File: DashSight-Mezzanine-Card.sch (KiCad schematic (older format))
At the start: 60 parts, among them IC1 ELM327, J1 OBD2-DB9_Male, P1 CONN_02X20, Q1 2N3904, Q2 2N3906, Q3 2N3906, Q4 2N3904, Q5 2N3904, Q6 2N3904, Q7 2N3904, U1 MCP2561-E/P, U2 LM317L_TO92, Y1 4.0MHz

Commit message: sch: Update for the new Pine board
Signed-off-by: Alistair Francis <alistair@alistair23.me>
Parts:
- removed LD1, LD2, LD3, LD4, LD5: LD_1C2A, Opto-Devices:LaserDiode_TO3.3(D3.3)-3, symbol Device:Laserdiode_1C2A
- removed P1: CONN_02X20, 96boards:Pin_Header_Straight_2x20_Pitch2mm, symbol DashSight-Mezzanine-Card-rescue:CONN_02X20
- removed R1, R22, R23, R24, R29: 470, Resistors_SMD:R_0603_HandSoldering, symbol Device:R
- added J?: Pi2 Connector, symbol Connector_Generic:Conn_02x20_Odd_Even
- added J?: Euler Connector, symbol Connector_Generic:Conn_02x17_Odd_Even
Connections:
- net labels added: +3.3V, UART2_RX, UART2_TX, UART3_RX, UART3_TX
- net labels removed: UART0_RX, UART0_TX
- wire segments 174 -> 151
- no-connect marks 34 -> 1
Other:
- note removed: "96-Boards Pin Header"
- moved on the sheet: C1, C2, C3, C4, C5, C6, D1, D2, D3, D4, IC1, J1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

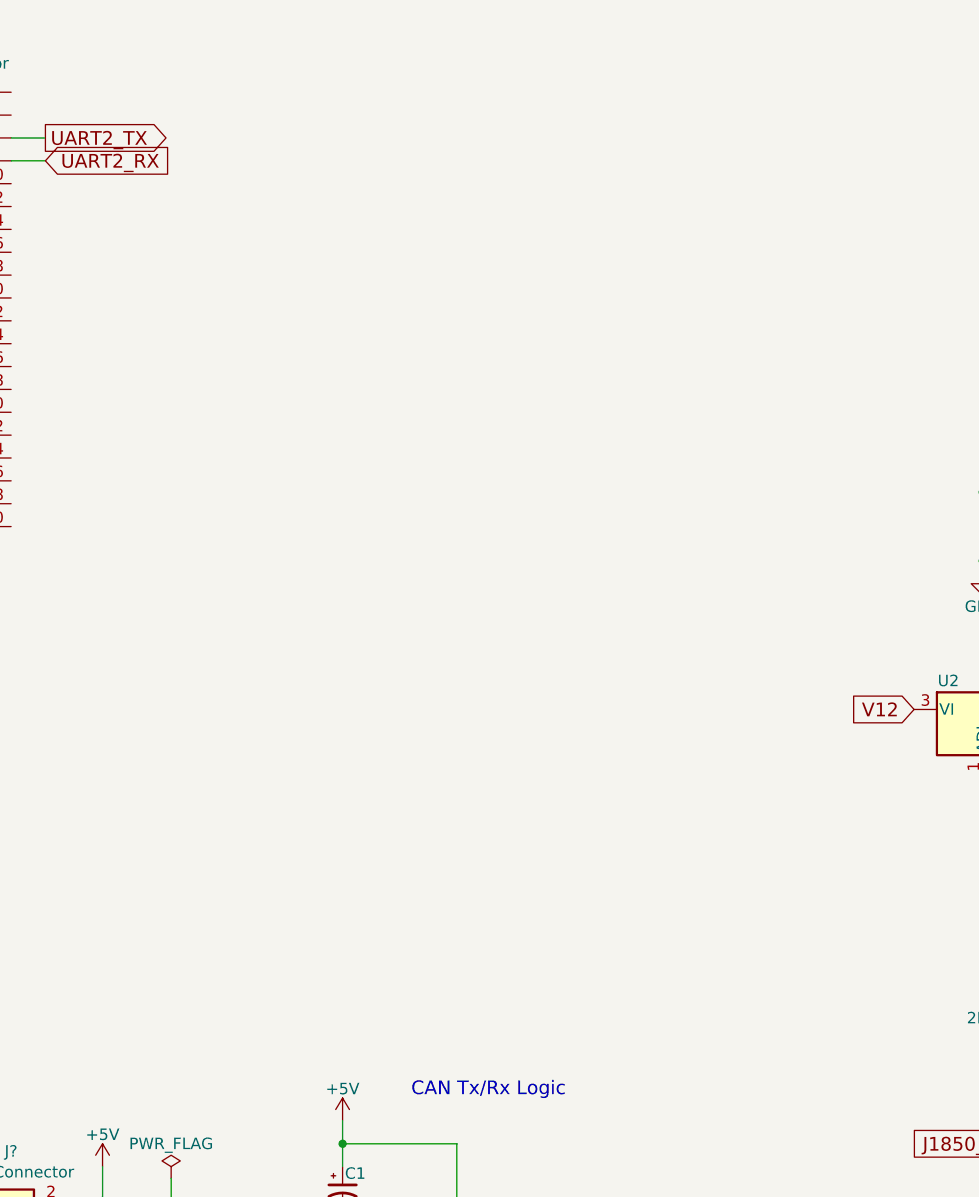
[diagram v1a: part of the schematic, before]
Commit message: Update with the GPS IC
Signed-off-by: Alistair Francis <alistair@alistair23.me>
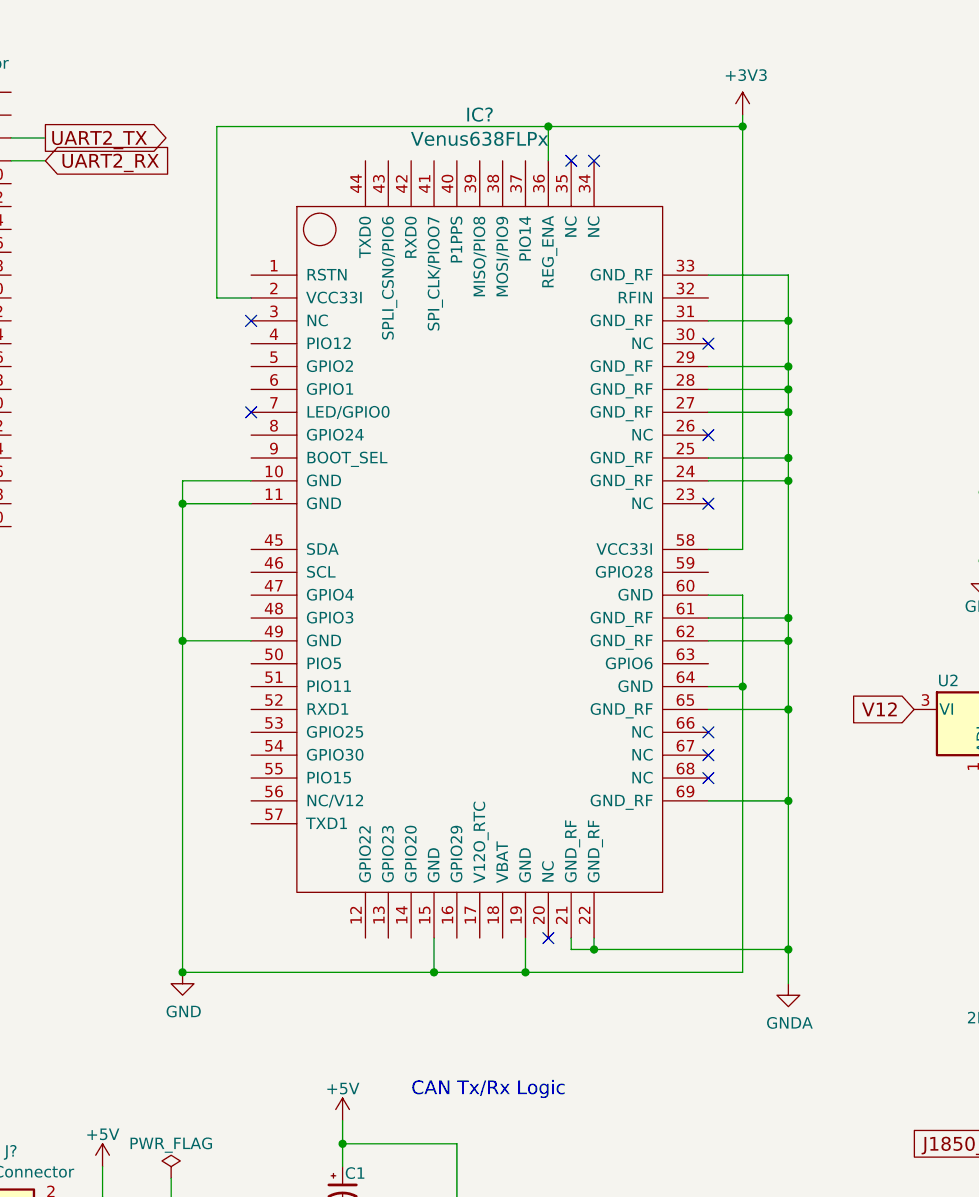
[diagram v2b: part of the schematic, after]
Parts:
- added IC?: Venus638FLPx, symbol Venus638FLPx:Venus638FLPx
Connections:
- net +3V3: now also IC?.2 (VCC33I), IC?.36 (REG_ENA), IC?.58 (VCC33I)
- net GND: now also IC?.10 (GND), IC?.11 (GND), IC?.15 (GND), IC?.19 (GND), IC?.49 (GND), IC?.60 (GND), IC?.64 (GND)
- new net GNDA: IC?.21 (GND_RF), IC?.22 (GND_RF), IC?.24 (GND_RF), IC?.25 (GND_RF), IC?.27 (GND_RF), IC?.28 (GND_RF), IC?.29 (GND_RF), IC?.31 (GND_RF), IC?.33 (GND_RF), IC?.61 (GND_RF), IC?.62 (GND_RF), IC?.65 (GND_RF), IC?.69 (GND_RF)
- no-connect marks 1 -> 12
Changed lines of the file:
@@
 	2650 7100 2650 7200
 Connection ~ 6750 6350
+$Comp
+L Venus638FLPx:Venus638FLPx IC?
+U 1 1 5BF87A18
+P 3450 3000
+F 0 "IC?" H 3450 5000 60  0000 C CNN
+F 1 "Venus638FLPx" H 3450 4894 60  0000 C CNN
+F 2 "" H 3450 3100 60  0001 C CNN
+F 3 "" H 3450 3100 60  0001 C CNN
+	1    3450 3000
+	1    0    0    -1
+$EndComp
+$Comp
+L power:+3V3 #PWR?
+U 1 1 5BF87D67
+P 4600 1000
+F 0 "#PWR?" H 4600 850 50  0001 C CNN
+F 1 "+3V3" H 4615 1173 50  0000 C CNN
+F 2 "" H 4600 1000 50  0001 C CNN
+F 3 "" H 4600 1000 50  0001 C CNN
+	1    4600 1000
+	1    0    0    -1
+$EndComp
+Wire Wire Line
+	4450 2900 4600 2900
+Wire Wire Line
+	4600 2900 4600 1050
+Wire Wire Line
+	3750 1200 3750 1050
+Wire Wire Line
+	3750 1050 4600 1050
+Connection ~ 4600 1050
+Wire Wire Line
+	4600 1050 4600 1000
+Wire Wire Line
+	2450 1800 2300 1800
+Wire Wire Line
+	2300 1800 2300 1050
+Wire Wire Line
+	2300 1050 3750 1050
+Connection ~ 3750 1050
+$Comp
+L power:GND #PWR?
+U 1 1 5BF9BD48
+P 2150 4750
+F 0 "#PWR?" H 2150 4500 50  0001 C CNN
+F 1 "GND" H 2155 4577 50  0000 C CNN
+F 2 "" H 2150 4750 50  0001 C CNN
+F 3 "" H 2150 4750 50  0001 C CNN
+	1    2150 4750
+	1    0    0    -1
+$EndComp
+Wire Wire Line
+	3250 4600 3250 4750
+Wire Wire Line
+	3250 4750 2150 4750
+Wire Wire Line
+	3650 4600 3650 4750
+Wire Wire Line
+	3650 4750 3250 4750
+Connection ~ 3250 4750
+Wire Wire Line
+	2450 3300 2150 3300
+Wire Wire Line
+	2150 3300 2150 4750
+Connection ~ 2150 4750
+Wire Wire Line
+	2450 2700 2150 2700
+Wire Wire Line
+	2150 2700 2150 3300
+Connection ~ 2150 3300
+Wire Wire Line
+	2450 2600 2150 2600
+Wire Wire Line
+	2150 2600 2150 2700
+Connection ~ 2150 2700
+Wire Wire Line
+	4450 3500 4600 3500
+Wire Wire Line
+	4600 3500 4600 4750
+Wire Wire Line
+	4600 4750 3650 4750
+Connection ~ 3650 4750
+Wire Wire Line
+	4450 3100 4600 3100
+Wire Wire Line
+	4600 3100 4600 3500
+Connection ~ 4600 3500
+NoConn ~ 4450 2000
+NoConn ~ 4450 2700
+NoConn ~ 4450 3700
+NoConn ~ 4450 3800
+NoConn ~ 4450 3900
+NoConn ~ 3750 4600
+NoConn ~ 2450 1900
+NoConn ~ 3850 1200
+NoConn ~ 3950 1200
+NoConn ~ 4450 2400
+NoConn ~ 2450 2300
+$Comp
+L power:GNDA #PWR?
+U 1 1 5C031CDD
+P 4800 4800
+F 0 "#PWR?" H 4800 4550 50  0001 C CNN
+F 1 "GNDA" H 4805 4627 50  0000 C CNN
+F 2 "" H 4800 4800 50  0001 C CNN
+F 3 "" H 4800 4800 50  0001 C CNN
+	1    4800 4800
+	1    0    0    -1
+$EndComp
+Wire Wire Line
+	4450 4000 4800 4000
+Wire Wire Line
+	4800 4000 4800 4650
+Wire Wire Line
+	4450 3600 4800 3600
+Wire Wire Line
+	4800 3600 4800 4000
+Connection ~ 4800 4000
+Wire Wire Line
+	4450 3300 4800 3300
+Wire Wire Line
+	4800 3300 4800 3600
+Connection ~ 4800 3600
+Wire Wire Line
+	4450 3200 4800 3200
+Wire Wire Line
+	4800 3200 4800 3300
+Connection ~ 4800 3300
+Wire Wire Line
+	4450 2600 4800 2600
+Wire Wire Line
+	4800 2600 4800 3200
+Connection ~ 4800 3200
+Wire Wire Line
+	4450 2500 4800 2500
+Wire Wire Line
+	4800 2500 4800 2600
+Connection ~ 4800 2600
+Wire Wire Line
+	4450 2300 4800 2300
+Wire Wire Line
+	4800 2300 4800 2500
+Connection ~ 4800 2500
+Wire Wire Line
+	4450 2200 4800 2200
+Wire Wire Line
+	4800 2200 4800 2300
+Connection ~ 4800 2300
+Wire Wire Line
+	4450 2100 4800 2100
+Wire Wire Line
+	4800 2100 4800 2200
+Connection ~ 4800 2200
+Wire Wire Line
+	4450 1900 4800 1900
+Wire Wire Line
+	4800 1900 4800 2100
+Connection ~ 4800 2100
+Wire Wire Line
+	4450 1700 4800 1700
+Wire Wire Line
+	4800 1700 4800 1900
+Connection ~ 4800 1900
+Wire Wire Line
+	3950 4600 3950 4650
+Wire Wire Line
+	3950 4650 4800 4650
+Connection ~ 4800 4650
+Wire Wire Line
+	4800 4650 4800 4800
+Wire Wire Line
+	3850 4600 3850 4650
+Wire Wire Line
+	3850 4650 3950 4650
+Connection ~ 3950 4650
 $EndSCHEMATC

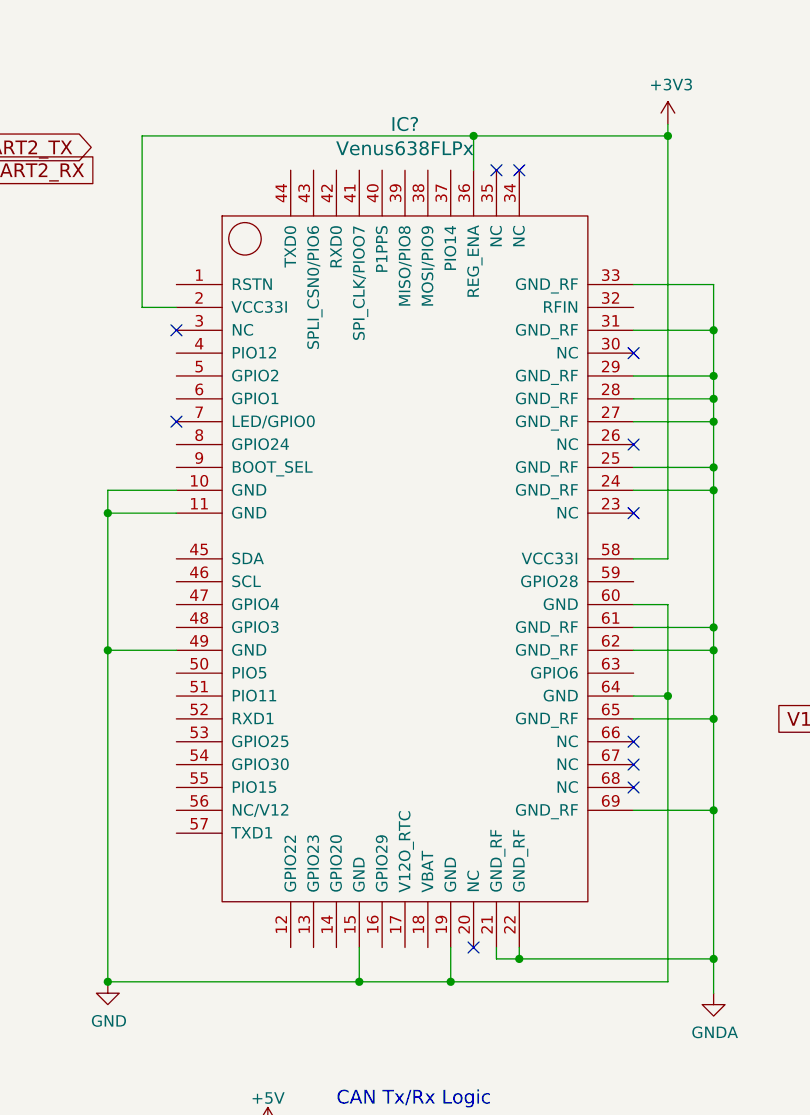
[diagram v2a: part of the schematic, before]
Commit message: More GPS connection updates
Signed-off-by: Alistair Francis <alistair@alistair23.me>
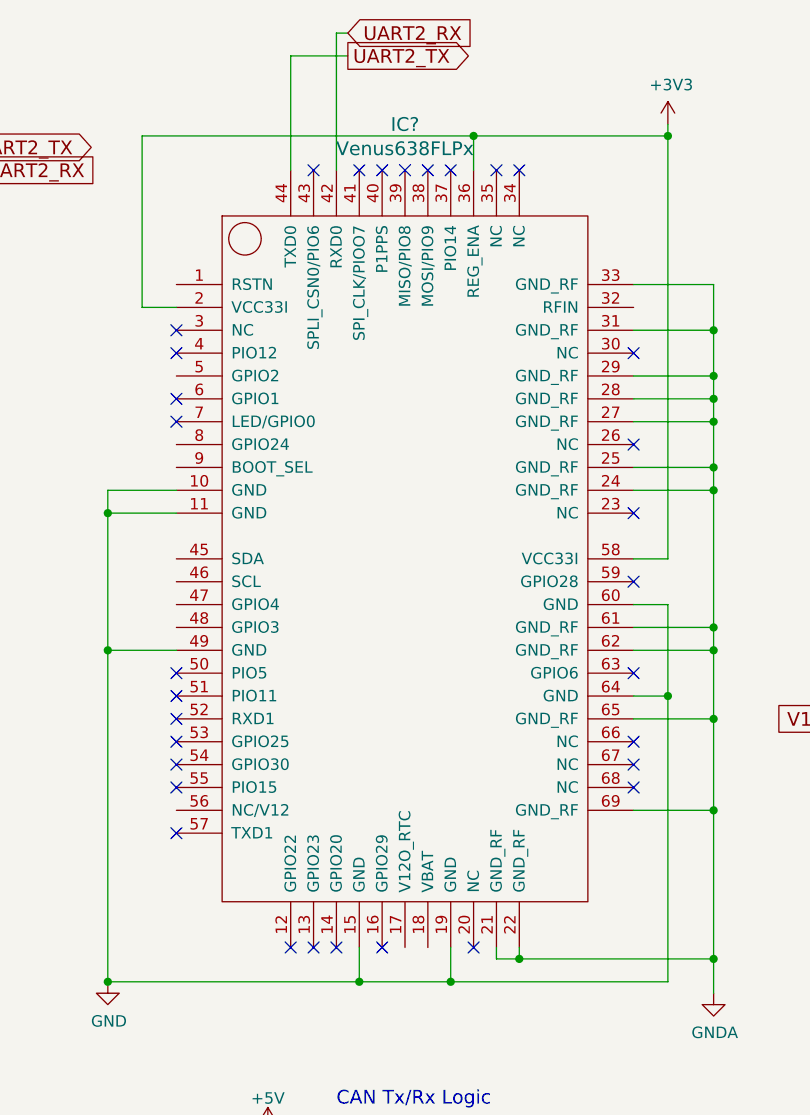
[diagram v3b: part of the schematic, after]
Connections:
- net UART2_RX: now also IC?.42 (RXD0)
- net UART2_TX: now also IC?.44 (TXD0)
- no-connect marks 12 -> 33
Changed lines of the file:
@@
 	3850 4650 3950 4650
 Connection ~ 3950 4650
+NoConn ~ 2450 3700
+NoConn ~ 4450 3000
+NoConn ~ 3350 4600
+NoConn ~ 2450 3800
+NoConn ~ 3050 4600
+NoConn ~ 2950 4600
+NoConn ~ 3150 4600
+NoConn ~ 2450 3900
+NoConn ~ 3650 1200
+NoConn ~ 2450 2000
+NoConn ~ 2450 3500
+NoConn ~ 4450 3400
+NoConn ~ 2450 2200
+Text GLabel 3200 600  2    60   Input ~ 0
+UART2_RX
+Text GLabel 3200 700  2    60   Output ~ 0
+UART2_TX
+Wire Wire Line
+	3150 1200 3150 600
+Wire Wire Line
+	3150 600  3200 600
+Wire Wire Line
+	3200 700  2950 700
+Wire Wire Line
+	2950 700  2950 1200
+NoConn ~ 2450 3400
+NoConn ~ 2450 3600
+NoConn ~ 2450 4100
+NoConn ~ 3450 1200
+NoConn ~ 3550 1200
+NoConn ~ 3050 1200
+NoConn ~ 3250 1200
+NoConn ~ 3350 1200
 $EndSCHEMATC

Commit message: Finalise schematics
Signed-off-by: Alistair Francis <alistair@alistair23.me>
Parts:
- added C1: 1uF, Capacitors_SMD:C_0603_HandSoldering, symbol Device:CP1
- added C5: 22pF, Capacitors_SMD:C_0603_HandSoldering, symbol Device:CP1
- added J3: Conn_Coaxial, symbol Connector:Conn_Coaxial
- added L1: 33nH, symbol pspice:INDUCTOR
- added R1: 33K, Resistors_SMD:R_1206_HandSoldering, symbol Device:R
- added R2, R4: 10K, Resistors_SMD:R_1206_HandSoldering, symbol Device:R
- gave numbers to parts that had none: 3
- renumbered C1 to C2, C2 to C3, C3 to C4, C4 to C6, C5 to C7, C6 to C8, D2 to D1, D3 to D2, D1 to D3, IC1 to IC2, J1 to J4, R8 to R10, R9 to R11, R10 to R12, R11 to R13, R12 to R14, R13 to R15, R14 to R16, R15 to R17, R16 to R18, R17 to R19, R18 to R20, R19 to R21, R20 to R22, R21 to R23, R25 to R24, R26 to R25, R27 to R26, R28 to R27, R30 to R28, R31 to R29, R2 to R3, R32 to R30, R3 to R5, R4 to R6, R5 to R7, R6 to R8, R7 to R9
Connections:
- net GNDA is gone; now on net GND: IC1.21 (GND_RF), IC1.22 (GND_RF), IC1.24 (GND_RF), IC1.25 (GND_RF), IC1.27 (GND_RF), IC1.28 (GND_RF), IC1.29 (GND_RF), IC1.31 (GND_RF), IC1.33 (GND_RF), IC1.61 (GND_RF), IC1.62 (GND_RF), IC1.65 (GND_RF), IC1.69 (GND_RF)
- net +3V3: now also IC1.18 (VBAT), C5.1, L1.2, R1.1
- net GND: now also IC1.8 (GPIO24), C1.2, C5.2, J3.2 (Ext), R2.2
- net UART2_RX: now also R4.1; no longer IC1.42 (RXD0)
- net UART2_TX: now also J1.10 (Pin_10); no longer J1.6 (Pin_6)
- net at IC1.1 (RSTN): now also C1.1, R1.2
- net at IC1.32 (RFIN): now also J3.1 (In), L1.1
- net at IC1.9 (BOOT_SEL): now also R2.1
- new net: IC1.42 (RXD0), R4.2
- no-connect marks 33 -> 110
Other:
- moved on the sheet: J1, J2

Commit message: sch: Update PCB components
Signed-off-by: Alistair Francis <alistair@alistair23.me>
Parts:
- C1, C2, C8: footprint Capacitors_SMD:C_0603_HandSoldering -> Capacitors_SMD:C_0402
- C3, C4, C5, C6, C7: footprint Capacitors_SMD:C_0603_HandSoldering -> Capacitors_SMD:C_0603
- D1, D2, D3, D4: footprint Diodes_SMD:D_SOD-123 -> Diodes_SMD:D_SMA
- IC1: footprint (none) -> Crystals:Crystal_SMD_SeikoEpson_MA505-2pin_12.7x5.1mm
- J1: footprint (none) -> Pin_Headers:Pin_Header_Straight_2x20_Pitch2.54mm
- J2: footprint (none) -> Pin_Headers:Pin_Header_Straight_2x16_Pitch2.54mm
- J3: footprint (none) -> Connectors:SMA_THT_Jack_Straight
- L1: footprint (none) -> Inductors_SMD:L_0603
- R1, R10, R11, R12, R14, R18, R19, R2, R21, R23, R26, R27, R4, R9: footprint Resistors_SMD:R_1206_HandSoldering -> Resistors_SMD:R_0603
- R13, R29, R30, R5, R6, R8: footprint Resistors_SMD:R_0603_HandSoldering -> Resistors_SMD:R_0603
- R15, R16, R17, R20, R22, R24, R25, R28, R3, R7: footprint Resistors_SMD:R_0201 -> Resistors_SMD:R_0603

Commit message: sch: Finish setting the PCB footprints
Signed-off-by: Alistair Francis <alistair@alistair23.me>
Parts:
- IC1: footprint Crystals:Crystal_SMD_SeikoEpson_MA505-2pin_12.7x5.1mm -> DashSight-PCB-Footprints:Venus638FLPx
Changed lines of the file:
@@
 F 0 "IC1" H 3450 5000 60  0000 C CNN
 F 1 "Venus638FLPx" H 3450 4894 60  0000 C CNN
-F 2 "Crystals:Crystal_SMD_SeikoEpson_MA505-2pin_12.7x5.1mm" H 3450 3100 60  0001 C CNN
+F 2 "DashSight-PCB-Footprints:Venus638FLPx" H 3450 3100 60  0001 C CNN
 F 3 "" H 3450 3100 60  0001 C CNN
 	1    3450 3000

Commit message: sch: Fix wrong number of pins
Signed-off-by: Alistair Francis <alistair@alistair23.me>
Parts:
- J2: footprint Pin_Headers:Pin_Header_Straight_2x16_Pitch2.54mm -> Pin_Headers:Pin_Header_Straight_2x17_Pitch2.54mm
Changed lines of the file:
@@
 F 0 "J2" H 1100 7567 50  0000 C CNN
 F 1 "Euler Connector" H 1100 7476 50  0000 C CNN
-F 2 "Pin_Headers:Pin_Header_Straight_2x16_Pitch2.54mm" H 1050 6550 50  0001 C CNN
+F 2 "Pin_Headers:Pin_Header_Straight_2x17_Pitch2.54mm" H 1050 6550 50  0001 C CNN
 F 3 "~" H 1050 6550 50  0001 C CNN
 	1    1050 6550

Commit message: pch: Finalise the PCB
Signed-off-by: Alistair Francis <alistair@alistair23.me>
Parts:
- J4: footprint Connectors_DSub:DSUB-9_Male_Horizontal_Pitch2.77x2.84mm_EdgePinOffset4.94mm_Housed_MountingHolesOffset7.48mm -> DashSight-PCB-Footprints:OBD2-Connector
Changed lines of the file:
@@
 F 0 "J4" H 9750 2100 50  0000 C CNN
 F 1 "OBD2-DB9_Male" H 9750 2025 50  0000 C CNN
-F 2 "Connectors_DSub:DSUB-9_Male_Horizontal_Pitch2.77x2.84mm_EdgePinOffset4.94mm_Housed_MountingHolesOffset7.48mm" H 9750 1450 50  0001 C CNN
+F 2 "DashSight-PCB-Footprints:OBD2-Connector" H 9750 1450 50  0001 C CNN
 F 3 "" H 9750 1450 50  0001 C CNN
 	1    9750 1450
